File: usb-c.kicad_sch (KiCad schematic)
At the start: 15 parts, among them IC1 TCPP01-M12, IC2 USBLC6-2SC6, IC3 632723100011, Q1 STL11N3LLH6

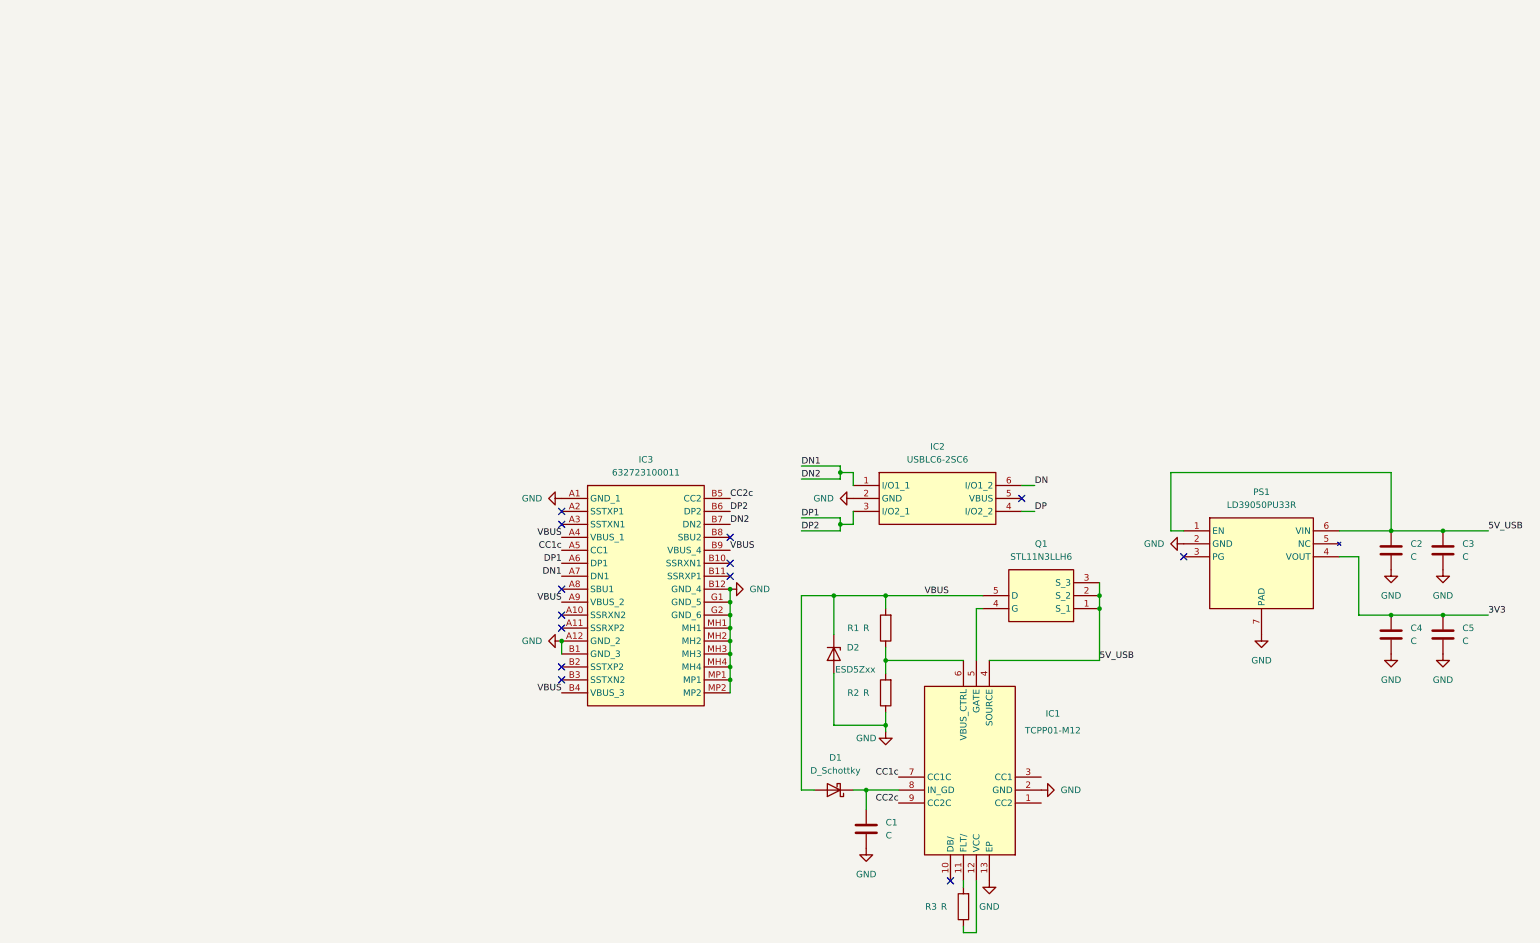
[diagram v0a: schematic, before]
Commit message: Add block diagram in a sheet
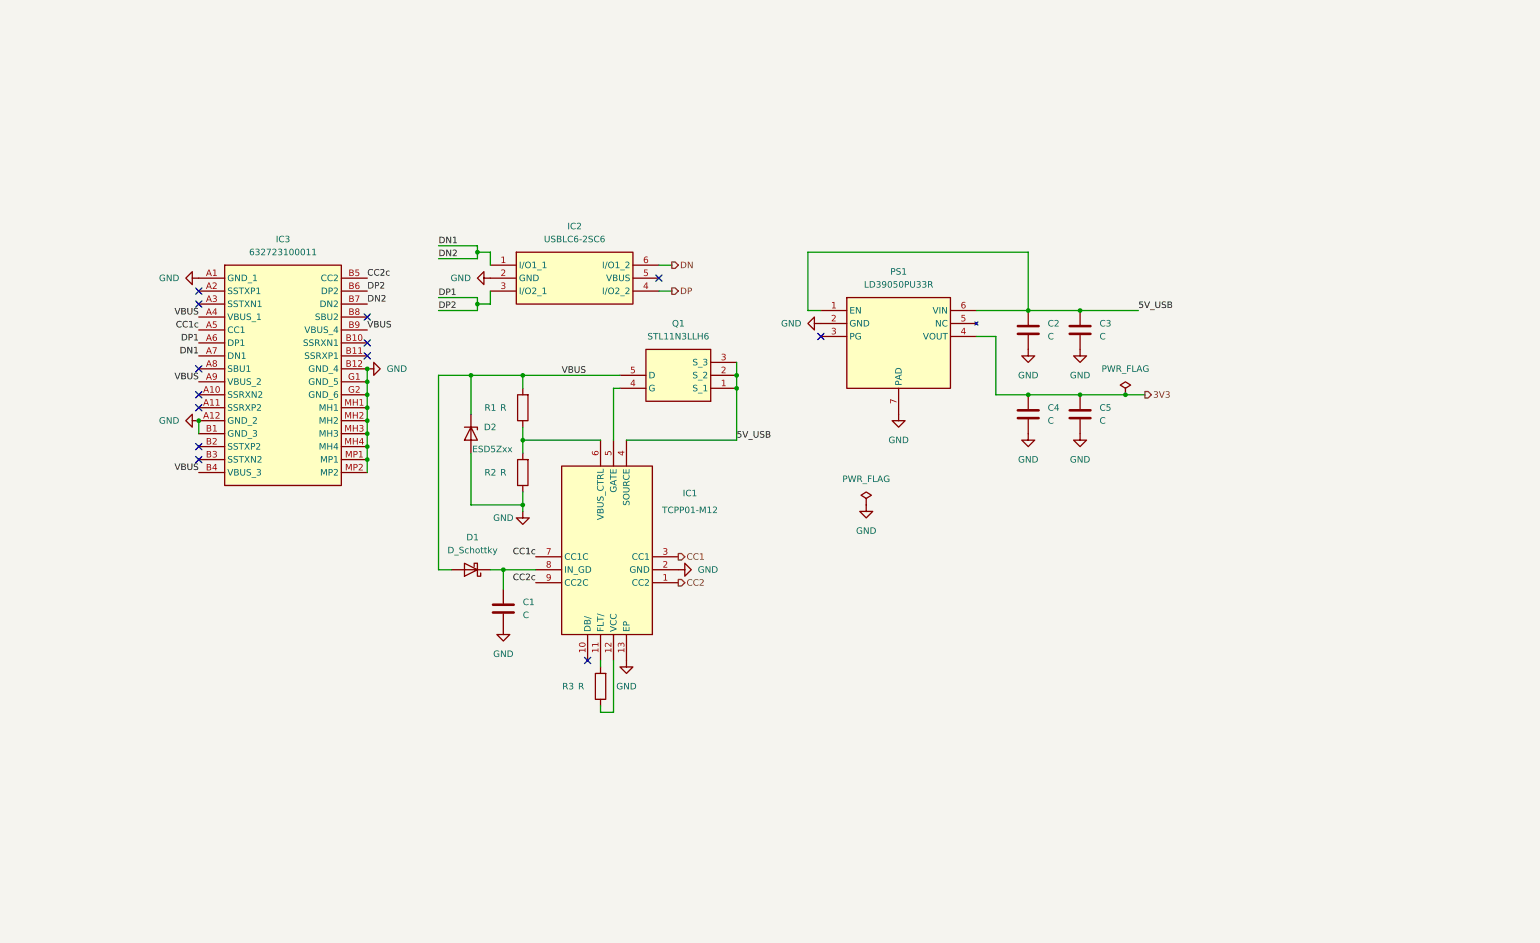
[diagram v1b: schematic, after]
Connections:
- net CC2: now reaches IC1.1 (CC2)
- net CC1: now reaches IC1.3 (CC1)
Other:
- moved on the sheet: C1, C2, C3, C4, C5, D1, D2, IC1, IC2, IC3, PS1, Q1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

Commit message: Test hierarchical labels on Kicad
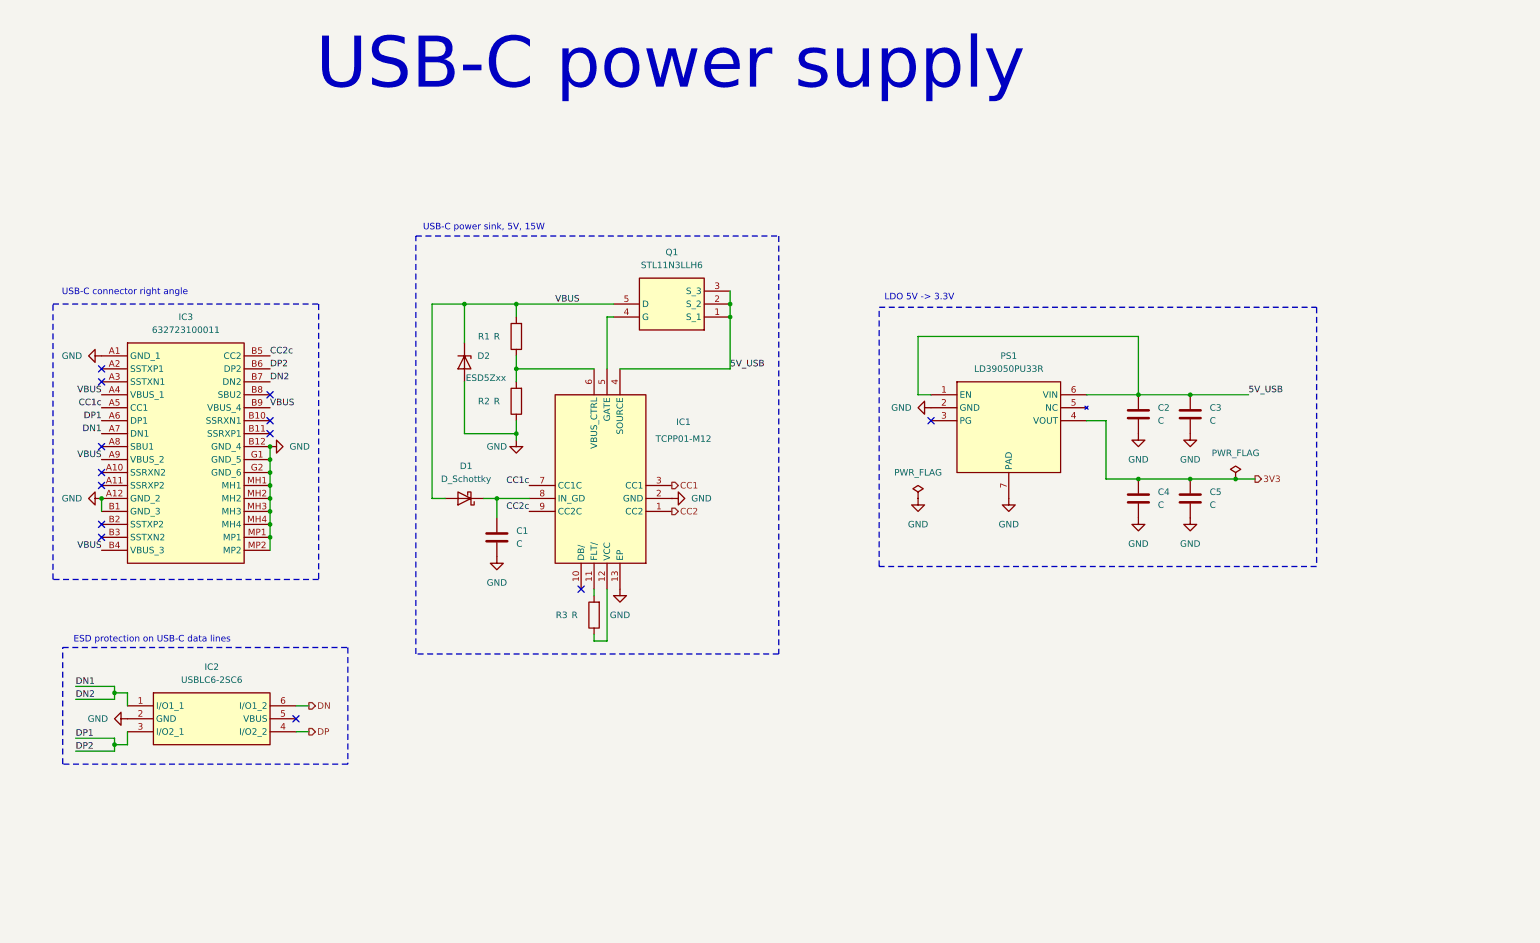
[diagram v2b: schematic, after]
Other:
- note added: "ESD protection on USB-C data lines"
- note added: "LDO 5V -> 3.3V"
- note added: "USB-C connector right angle"
- note added: "USB-C power sink, 5V, 15W"
- note added: "USB-C power supply"
- moved on the sheet: C1, C2, C3, C4, C5, D1, D2, IC1, IC2, IC3, PS1, Q1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

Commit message: Beginning of all signals definition
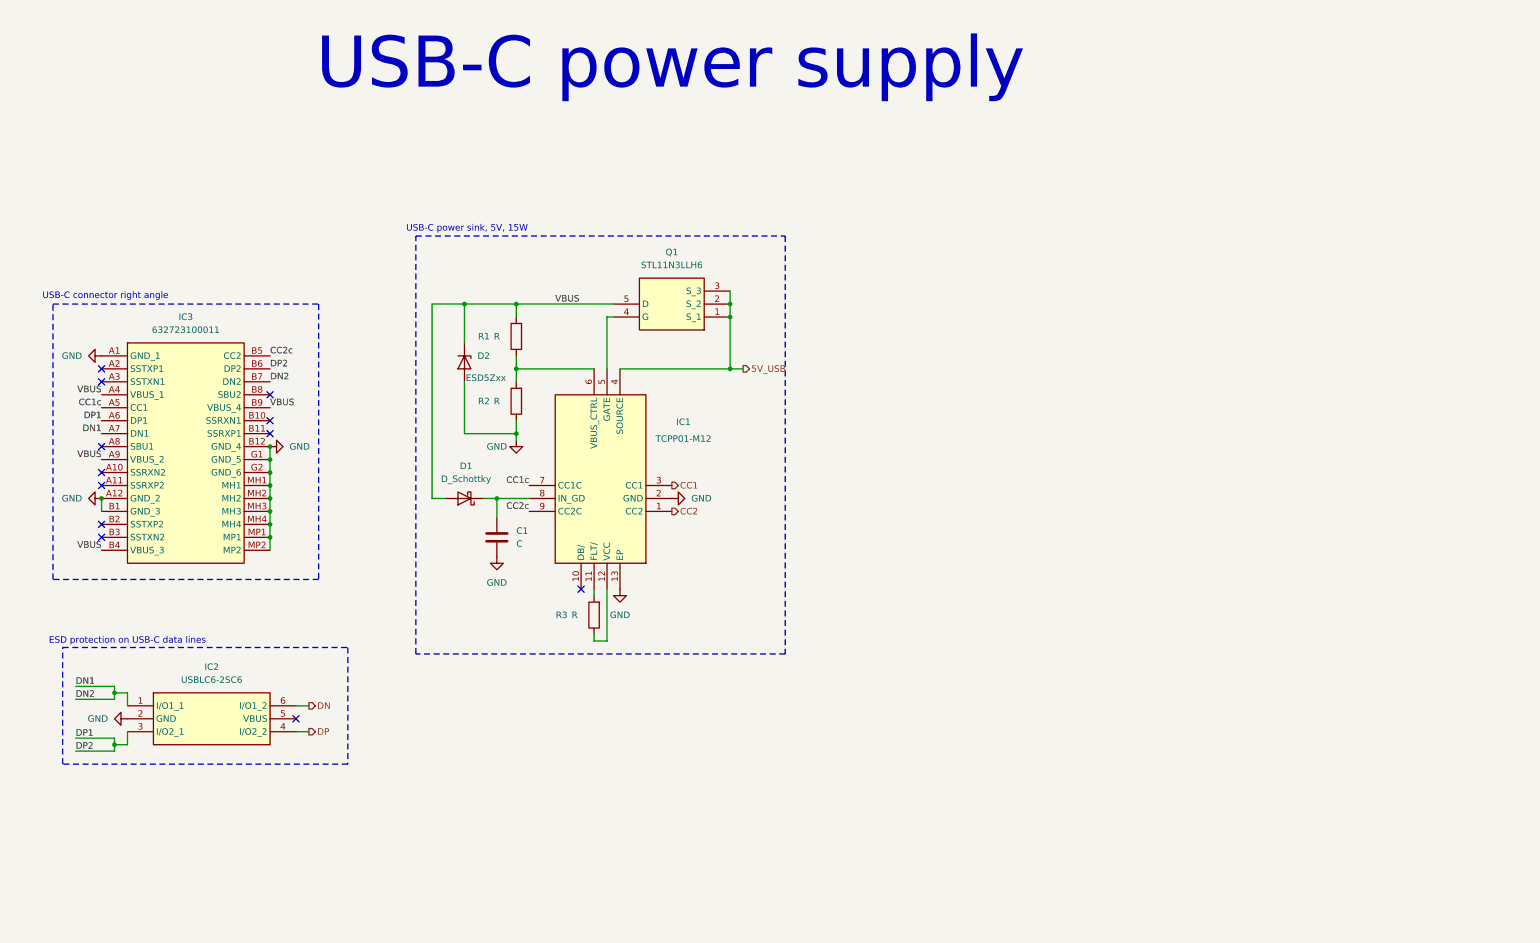
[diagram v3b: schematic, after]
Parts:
- removed C2, C3, C4, C5: C, Capacitor_SMD:C_0603_1608Metric_Pad1.08x0.95mm_HandSolder, symbol Device:C
- removed PS1: LD39050PU33R, SON95P300X300X100-7N-D, symbol weather-station-poc-sym:LD39050PU33R
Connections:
- no-connect marks 13 -> 12
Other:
- note removed: "LDO 5V -> 3.3V"

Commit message: Define power flags
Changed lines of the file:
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@@
 	)
 	(rectangle
-		(start 24.765 71.12)
+		(start 22.86 71.12)
 		(end 76.835 125.095)
 		(stroke
@@
 	(text "USB-C connector right angle\n"
 		(exclude_from_sim no)
-		(at 35.052 69.596 0)
+		(at 33.274 69.596 0)
 		(effects
 			(font
@@
 	)
 	(junction
+		(at 34.29 81.28)
+		(diameter 0)
+		(color 0 0 0 0)
+	)
+	(junction
 		(at 157.48 71.12)
 		(diameter 0)
@@
 	)
 	(junction
+		(at 129.54 71.12)
+		(diameter 0)
+		(color 0 0 0 0)
+	)
+	(junction
 		(at 67.31 99.06)
 		(diameter 0)
@@
 	(wire
 		(pts
+			(xy 129.54 71.12) (xy 134.62 71.12)
+		)
+		(stroke
+			(width 0)
+			(type default)
+		)
+	)
+	(wire
+		(pts
 			(xy 133.35 73.66) (xy 134.62 73.66)
 		)
@@
 	(wire
 		(pts
-			(xy 115.57 71.12) (xy 134.62 71.12)
+			(xy 115.57 71.12) (xy 129.54 71.12)
 		)
 		(stroke
@@
 		(pts
 			(xy 115.57 81.28) (xy 115.57 83.82)
+		)
+		(stroke
+			(width 0)
+			(type default)
+		)
+	)
+	(wire
+		(pts
+			(xy 31.75 81.28) (xy 34.29 81.28)
 		)
 		(stroke
@@
 			)
 			(justify left)
+		)
+	)
+	(symbol
+		(lib_id "power:PWR_FLAG")
+		(at 34.29 81.28 0)
+		(unit 1)
+		(exclude_from_sim no)
+		(in_bom yes)
+		(on_board yes)
+		(dnp no)
+		(fields_autoplaced yes)
+		(property "Reference" "#FLG02"
+			(at 34.29 79.375 0)
+			(effects
+				(font
+					(size 1.27 1.27)
+				)
+				(hide yes)
+			)
+		)
+		(property "Value" "PWR_FLAG"
+			(at 34.29 76.2 0)
+			(effects
+				(font
+					(size 1.27 1.27)
+				)
+			)
+		)
+		(property "Footprint" ""
+			(at 34.29 81.28 0)
+			(effects
+				(font
+					(size 1.27 1.27)
+				)
+				(hide yes)
+			)
+		)
+		(property "Datasheet" "~"
+			(at 34.29 81.28 0)
+			(effects
+				(font
+					(size 1.27 1.27)
+				)
+				(hide yes)
+			)
+		)
+		(property "Description" "Special symbol for telling ERC where power comes from"
+			(at 34.29 81.28 0)
+			(effects
+				(font
+					(size 1.27 1.27)
+				)
+				(hide yes)
+			)
+		)
+		(pin "1"
+		)
+		(instances
+			(project "weather-station-poc"
+				(path "/38eb53bb-294e-46e4-ad59-fd355ca373b9/336d3e95-9b5f-4d37-8b5a-efff814cf96e"
+					(reference "#FLG02")
+					(unit 1)
+				)
+			)
 		)
 	)
@@
 	(symbol
 		(lib_id "power:GND")
-		(at 34.29 81.28 270)
+		(at 31.75 81.28 270)
 		(unit 1)
 		(exclude_from_sim no)
@@
 		(fields_autoplaced yes)
 		(property "Reference" "#PWR09"
-			(at 27.94 81.28 0)
+			(at 25.4 81.28 0)
 			(effects
 				(font
@@
 		)
 		(property "Value" "GND"
-			(at 30.48 81.2799 90)
+			(at 27.94 81.2799 90)
 			(effects
 				(font
@@
 		)
 		(property "Footprint" ""
-			(at 34.29 81.28 0)
+			(at 31.75 81.28 0)
 			(effects
 				(font
@@
 		)
 		(property "Datasheet" ""
-			(at 34.29 81.28 0)
+			(at 31.75 81.28 0)
 			(effects
 				(font
@@
 		)
 		(property "Description" "Power symbol creates a global label with name \"GND\" , ground"
-			(at 34.29 81.28 0)
+			(at 31.75 81.28 0)
 			(effects
 				(font
@@
 					(unit 1)
 				)
+			)
+		)
+	)
+	(symbol
+		(lib_id "power:PWR_FLAG")
+		(at 129.54 71.12 0)
+		(unit 1)
+		(exclude_from_sim no)
+		(in_bom yes)
+		(on_board yes)
+		(dnp no)
+		(fields_autoplaced yes)
+		(property "Reference" "#FLG01"
+			(at 129.54 69.215 0)
+			(effects
+				(font
+					(size 1.27 1.27)
+				)
+				(hide yes)
+			)
+		)
+		(property "Value" "PWR_FLAG"
+			(at 129.54 66.04 0)
+			(effects
+				(font
+					(size 1.27 1.27)
+				)
+			)
+		)
+		(property "Footprint" ""
+			(at 129.54 71.12 0)
+			(effects
+				(font
+					(size 1.27 1.27)
+				)
+				(hide yes)
+			)
+		)
+		(property "Datasheet" "~"
+			(at 129.54 71.12 0)
+			(effects
+				(font
+					(size 1.27 1.27)
+				)
+				(hide yes)
+			)
+		)
+		(property "Description" "Special symbol for telling ERC where power comes from"
+			(at 129.54 71.12 0)
+			(effects
+				(font
+					(size 1.27 1.27)
+				)
+				(hide yes)
+			)
+		)
+		(pin "1"
+		)
+		(instances
+			(project ""
+				(path "/38eb53bb-294e-46e4-ad59-fd355ca373b9/336d3e95-9b5f-4d37-8b5a-efff814cf96e"
+					(reference "#FLG01")
+					(unit 1)
+				)

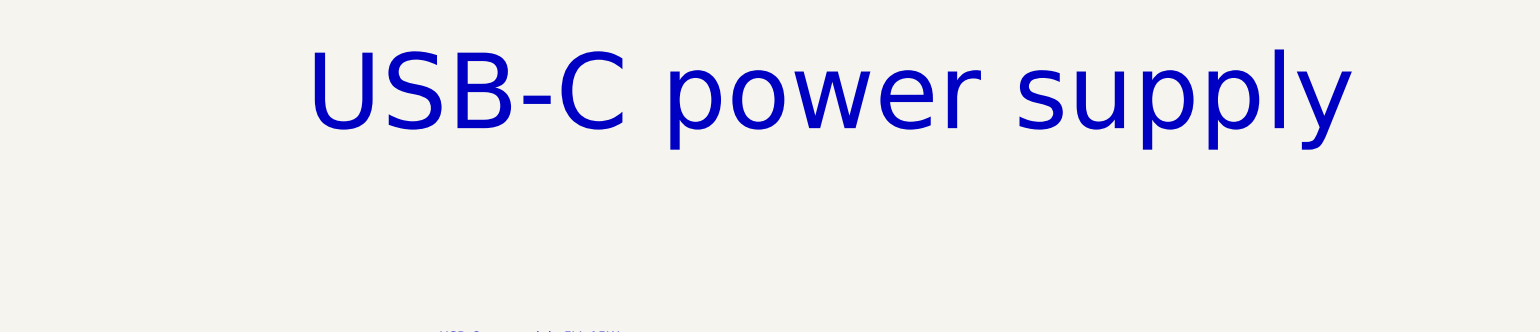
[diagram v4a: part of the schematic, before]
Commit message: Use local labels for RGB bus in folio and add title for all folio
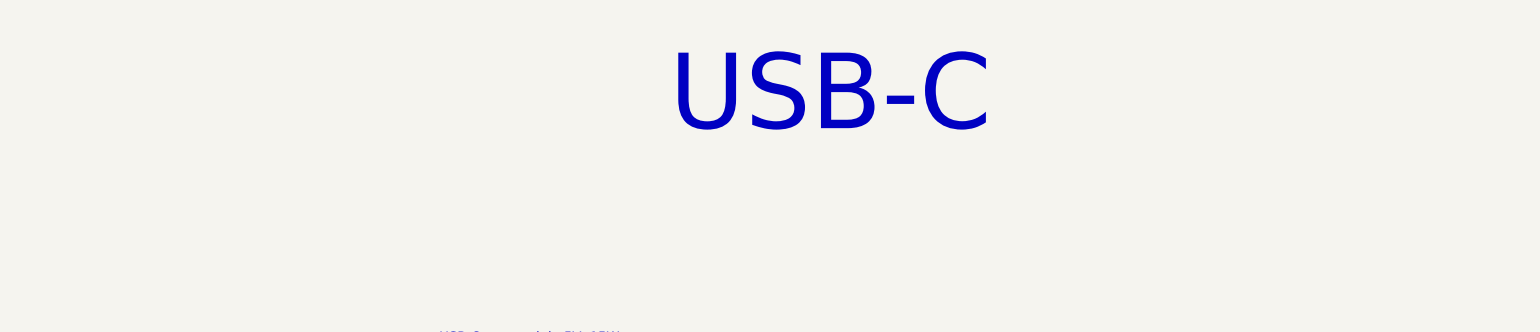
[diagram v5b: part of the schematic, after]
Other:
- note added: "USB-C"
- note removed: "USB-C power supply"
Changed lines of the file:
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@@
 		)
 	)
-	(text "USB-C power supply"
+	(text "USB-C"
 		(exclude_from_sim no)
 		(at 145.796 24.13 0)
